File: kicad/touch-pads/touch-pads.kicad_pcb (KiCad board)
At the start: 2 copper layers, 119.5 x 161 mm, 51 parts, among them J1 Conn_01x03_Socket, J2 Conn_01x06_Socket, J3 Conn_01x06_Socket, J4 Conn_01x03_Socket, J5 Conn_01x06_Socket, J6 Conn_01x06_Socket, K1 Conn_01x01, K2 Conn_01x01, K3 Conn_01x01, K4 Conn_01x01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

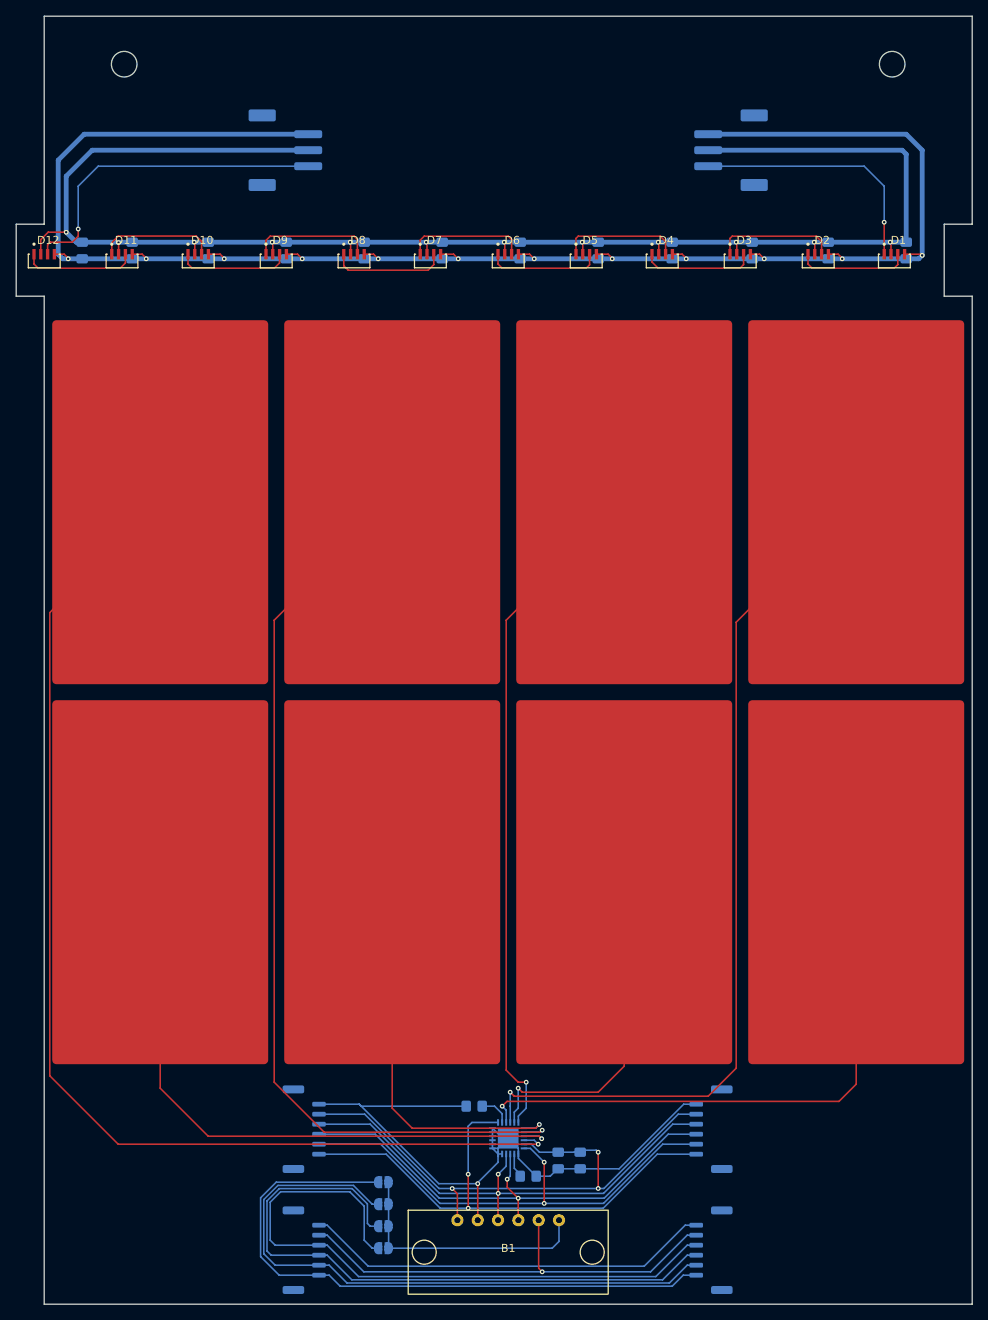
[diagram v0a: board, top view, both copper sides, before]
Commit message: update to kicad 9
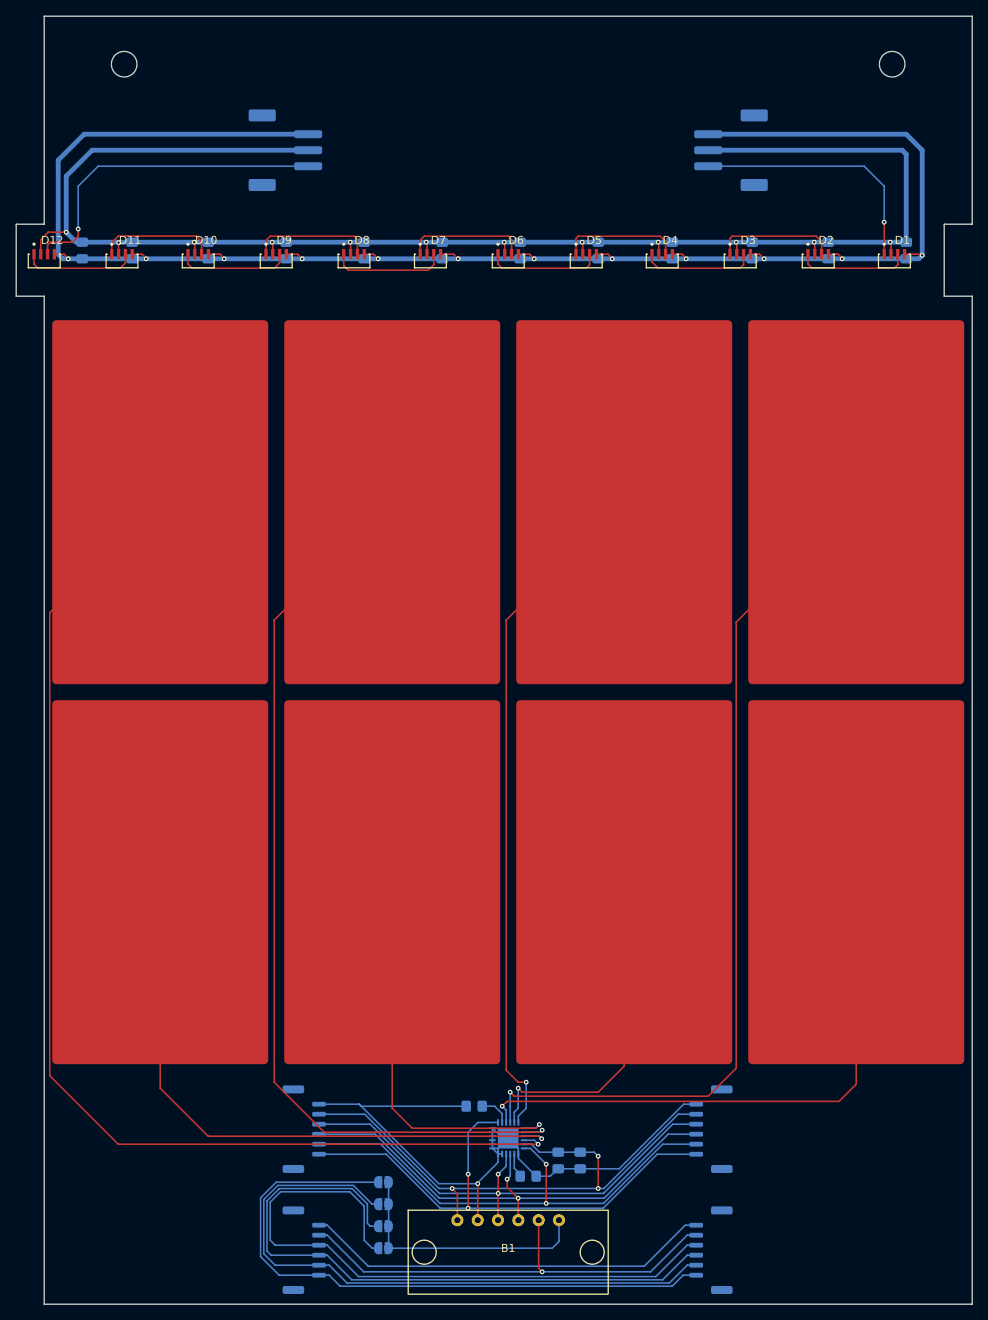
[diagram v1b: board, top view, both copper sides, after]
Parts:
- D1, D10, D11, D12, D2, D3, D4, D5, D6, D7, D8, D9: footprint WS2812B-4020:WS2812B-4020 -> WS2812B-4020:LED_WS2812B-4020
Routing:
- net +3.3V: track 73.5 -> 73.0 mm

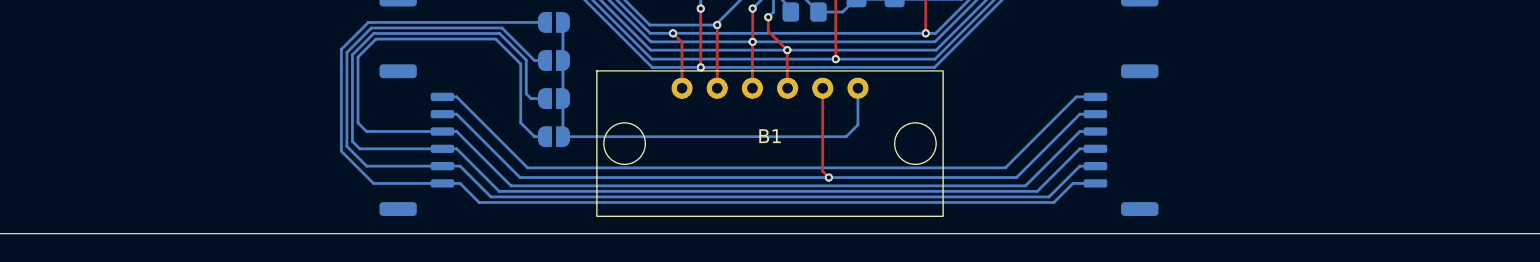
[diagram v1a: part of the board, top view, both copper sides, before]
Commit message: add mount holes
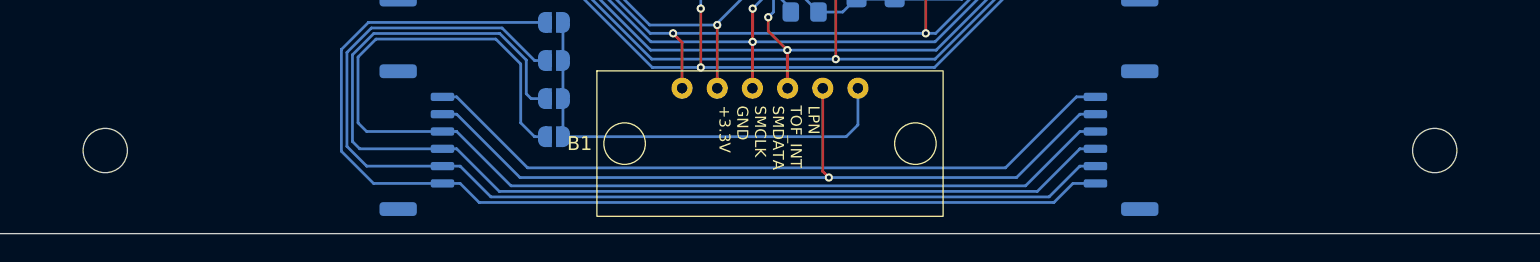
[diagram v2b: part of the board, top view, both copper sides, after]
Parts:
- added H3: MountingHole, MountingHole:MountingHole_3.2mm_M3, F.Cu at (215.2, 255.8)
- added H4: MountingHole, MountingHole:MountingHole_3.2mm_M3, F.Cu at (311.2, 255.8)
- moved G*** 173.3 mm to (224.2, 106.8)
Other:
- board text added: "LPN TOF_INT SMDATA SMCLK GND +3.3V"
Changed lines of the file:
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@@
 		(embedded_fonts no)
 	)
+	(footprint "MountingHole:MountingHole_3.2mm_M3"
+		(layer "F.Cu")
+		(at 311.25 255.75)
+		(descr "Mounting Hole 3.2mm, M3, no annular, generated by kicad-footprint-generator mountinghole.py")
+		(tags "mountinghole M3")
+		(property "Reference" "H4"
+			(at 0 -4.15 0)
+			(layer "F.SilkS")
+			(hide yes)
+			(effects
+				(font
+					(size 1 1)
+					(thickness 0.15)
+				)
+			)
+		)
+		(property "Value" "MountingHole"
+			(at 0 4.15 0)
+			(layer "F.Fab")
+			(effects
+				(font
+					(size 1 1)
+					(thickness 0.15)
+				)
+			)
+		)
+		(property "Datasheet" ""
+			(at 0 0 0)
+			(layer "F.Fab")
+			(hide yes)
+			(effects
+				(font
+					(size 1.27 1.27)
+					(thickness 0.15)
+				)
+			)
+		)
+		(property "Description" "Mounting Hole without connection"
+			(at 0 0 0)
+			(layer "F.Fab")
+			(hide yes)
+			(effects
+				(font
+					(size 1.27 1.27)
+					(thickness 0.15)
+				)
+			)
+		)
+		(property ki_fp_filters "MountingHole*")
+		(sheetname "/")
+		(sheetfile "touch-pads.kicad_sch")
+		(attr exclude_from_pos_files exclude_from_bom)
+		(fp_circle
+			(center 0 0)
+			(end 3.2 0)
+			(stroke
+				(width 0.15)
+				(type solid)
+			)
+			(fill no)
+			(layer "Cmts.User")
+		)
+		(fp_circle
+			(center 0 0)
+			(end 3.45 0)
+			(stroke
+				(width 0.05)
+				(type solid)
+			)
+			(fill no)
+			(layer "F.CrtYd")
+		)
+		(fp_text user "${REFERENCE}"
+			(at 0 0 0)
+			(layer "F.Fab")
+			(effects
+				(font
+					(size 1 1)
+					(thickness 0.15)
+				)
+			)
+		)
+		(pad "" np_thru_hole circle
+			(at 0 0)
+			(size 3.2 3.2)
+			(drill 3.2)
+			(layers "*.Cu" "*.Mask")
+		)
+		(embedded_fonts no)
+	)
 	(footprint "WS2812B-4020:LED_WS2812B-4020"
 		(layer "F.Cu")
@@
 		(embedded_fonts no)
 	)
+	(footprint "MountingHole:MountingHole_3.2mm_M3"
+		(layer "F.Cu")
+		(at 215.25 255.75)
+		(descr "Mounting Hole 3.2mm, M3, no annular, generated by kicad-footprint-generator mountinghole.py")
+		(tags "mountinghole M3")
+		(property "Reference" "H3"
+			(at 0 -4.15 0)
+			(layer "F.SilkS")
+			(hide yes)
+			(effects
+				(font
+					(size 1 1)
+					(thickness 0.15)
+				)
+			)
+		)
+		(property "Value" "MountingHole"
+			(at 0 4.15 0)
+			(layer "F.Fab")
+			(effects
+				(font
+					(size 1 1)
+					(thickness 0.15)
+				)
+			)
+		)
+		(property "Datasheet" ""
+			(at 0 0 0)
+			(layer "F.Fab")
+			(hide yes)
+			(effects
+				(font
+					(size 1.27 1.27)
+					(thickness 0.15)
+				)
+			)
+		)
+		(property "Description" "Mounting Hole without connection"
+			(at 0 0 0)
+			(layer "F.Fab")
+			(hide yes)
+			(effects
+				(font
+					(size 1.27 1.27)
+					(thickness 0.15)
+				)
+			)
+		)
+		(property ki_fp_filters "MountingHole*")
+		(sheetname "/")
+		(sheetfile "touch-pads.kicad_sch")
+		(attr exclude_from_pos_files exclude_from_bom)
+		(fp_circle
+			(center 0 0)
+			(end 3.2 0)
+			(stroke
+				(width 0.15)
+				(type solid)
+			)
+			(fill no)
+			(layer "Cmts.User")
+		)
+		(fp_circle
+			(center 0 0)
+			(end 3.45 0)
+			(stroke
+				(width 0.05)
+				(type solid)
+			)
+			(fill no)
+			(layer "F.CrtYd")
+		)
+		(fp_text user "${REFERENCE}"
+			(at 0 0 0)
+			(layer "F.Fab")
+			(effects
+				(font
+					(size 1 1)
+					(thickness 0.15)
+				)
+			)
+		)
+		(pad "" np_thru_hole circle
+			(at 0 0)
+			(size 3.2 3.2)
+			(drill 3.2)
+			(layers "*.Cu" "*.Mask")
+		)
+		(embedded_fonts no)
+	)
 	(footprint "VL53L5CX_Breakout:VL53L5CX_Breakout_Aliexpress"
 		(layer "F.Cu")
 		(at 263.25 255.25)
 		(property "Reference" "B1"
-			(at 0 -0.5 0)
+			(at -13.75 0 0)
 			(unlocked yes)
 			(layer "F.SilkS")
@@
 	(footprint "Logo:Snep_Copper"
 		(layer "B.Cu")
-		(at 314 255 180)
+		(at 224.25 106.75 180)
 		(property "Reference" "G***"
 			(at 0 0 0)
@@
 	)
 	(gr_line
+		(start 321.25 255.75)
+		(end 311.25 255.75)
+		(stroke
+			(width 0.1)
+			(type default)
+		)
+		(layer "Dwgs.User")
+	)
+	(gr_line
 		(start 230.25 112.5)
 		(end 205.25 112.5)
@@
 	)
 	(gr_line
+		(start 215.25 261.75)
+		(end 215.25 255.75)
+		(stroke
+			(width 0.1)
+			(type default)
+		)
+		(layer "Dwgs.User")
+	)
+	(gr_line
 		(start 219.75 130.75)
 		(end 222.25 130.75)
@@
 	)
 	(gr_line
+		(start 215.25 255.75)
+		(end 205.25 255.75)
+		(stroke
+			(width 0.1)
+			(type default)
+		)
+		(layer "Dwgs.User")
+	)
+	(gr_line
 		(start 234.25 127.25)
 		(end 263.25 127.25)
@@
 	)
 	(gr_line
+		(start 311.25 255.75)
+		(end 311.25 261.75)
+		(stroke
+			(width 0.1)
+			(type default)
+		)
+		(layer "Dwgs.User")
+	)
+	(gr_line
 		(start 205.25 138.75)
 		(end 206.75 138.75)
@@
 		(layer "Edge.Cuts")
 	)
+	(gr_text "LPN\nTOF_INT\nSMDATA\nSMCLK\nGND\n+3.3V"
+		(at 259.5 252.5 270)
+		(layer "F.SilkS")
+		(effects
+			(font
+				(size 0.8 0.8)
+				(thickness 0.15)
+			)
+			(justify left bottom)
+		)
+	)
 	(gr_text "GND\n+5V\nLED_DATA_IN"
